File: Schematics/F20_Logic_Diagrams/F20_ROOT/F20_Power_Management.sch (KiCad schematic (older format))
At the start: 9 parts, among them U11 Battery, U12 Cutoff_Switch, U13 Alternator, U14 Rectifier, U15 Starter_Relay, U16 Starter_Motor

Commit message: Added PDM Layout guide, updated Powertrain wiring, added a Master Connector Pinout guide, added TOC to LogicDiagrams pdf and rearranged them a bit.
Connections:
- new net: S1.~, U15.~ (Start)
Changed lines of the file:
@@
 $Descr A 11000 8500
 encoding utf-8
-Sheet 10 18
+Sheet 2 18
 Title "Fuses and Relays"
 Date "2020-01-28"

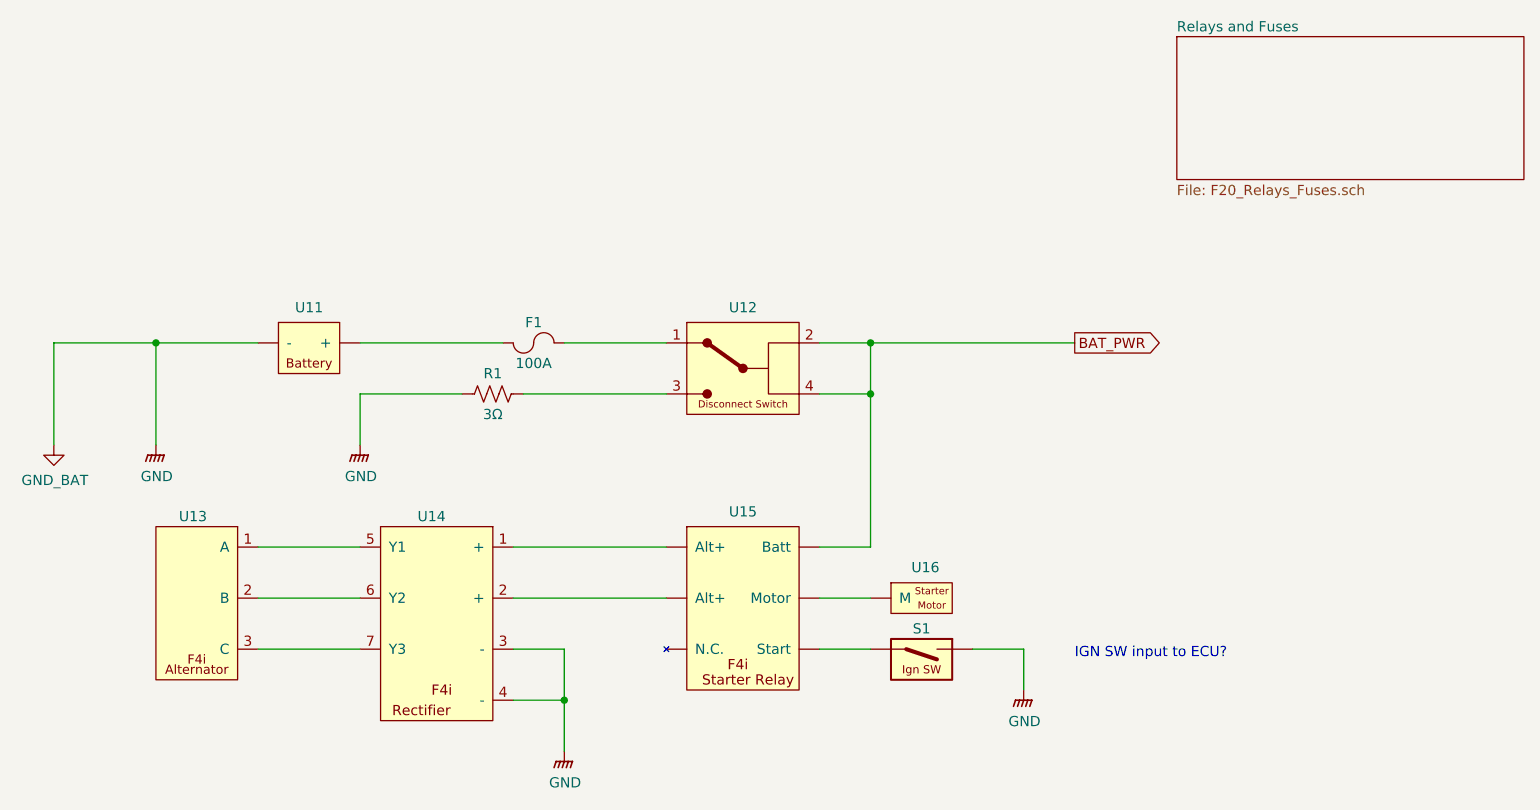
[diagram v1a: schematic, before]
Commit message: Re-annotated Logic Diagrams, pulled a BOM list based on Logic Diagrams
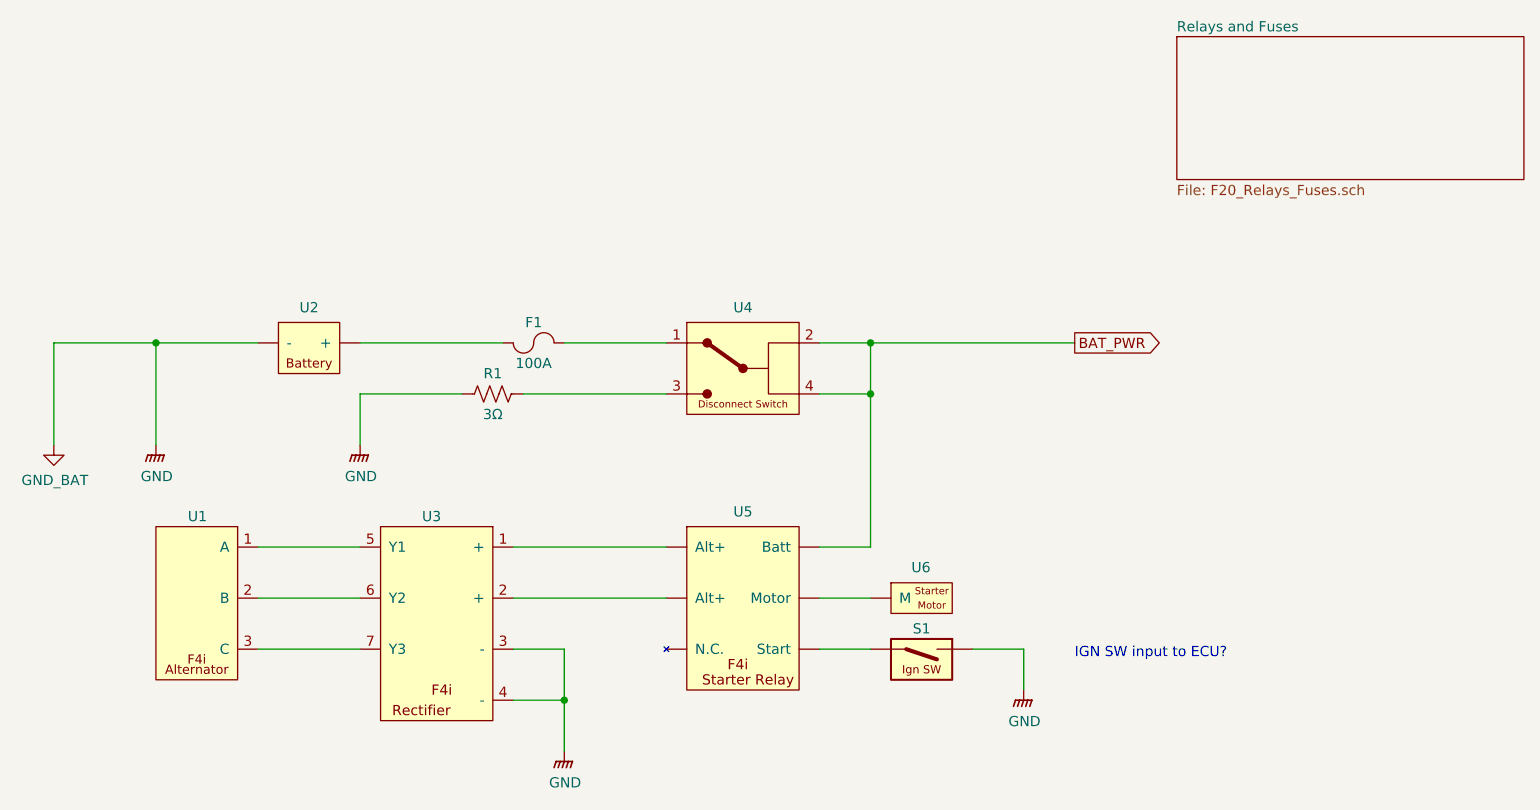
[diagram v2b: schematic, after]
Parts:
- renumbered U13 to U1, U11 to U2, U14 to U3, U12 to U4, U15 to U5, U16 to U6
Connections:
- new net: S1.~, U5.~ (Start)
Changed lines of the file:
@@
 BAT_PWR
 $Comp
-L FSAE_Library:Battery U11
+L FSAE_Library:Battery U2
 U 1 1 5E233AF7
 P 4000 3000
-F 0 "U11" H 3750 3173 50  0000 C CNN
+F 0 "U2" H 3750 3173 50  0000 C CNN
 F 1 "Battery" H 3750 3150 50  0001 C CNN
 F 2 "" H 3750 3150 50  0001 C CNN
@@
 	3000 3000 3500 3000
 $Comp
-L FSAE_Library:Cutoff_Switch U12
+L FSAE_Library:Cutoff_Switch U4
 U 1 1 5E237569
 P 5500 3000
-F 0 "U12" H 5875 3173 50  0000 C CNN
+F 0 "U4" H 5875 3173 50  0000 C CNN
 F 1 "Cutoff_Switch" H 5850 3150 50  0001 C CNN
 F 2 "" H 5850 3150 50  0001 C CNN
@@
 	4000 4000 3500 4000
 $Comp
-L FSAE_Library:Alternator U13
+L FSAE_Library:Alternator U?
 U 1 1 5E21541A
 P 3500 4000
-AR Path="/5E21541A" Ref="U13"  Part="1"
-AR Path="/5E1D1A8A/5E21541A" Ref="U13"  Part="1"
-F 0 "U13" H 3750 4150 50  0000 L CNN
+AR Path="/5E21541A" Ref="U?"  Part="1"
+AR Path="/5E1D1A8A/5E21541A" Ref="U1"  Part="1"
+F 0 "U1" H 3750 4150 50  0000 L CNN
 F 1 "Alternator" H 3800 4150 50  0001 C CNN
 F 2 "" H 3800 4150 50  0001 C CNN
@@
 $EndComp
 $Comp
-L FSAE_Library:Rectifier U14
+L FSAE_Library:Rectifier U3
 U 1 1 5E21334A
 P 4750 4000
-F 0 "U14" H 5150 4150 50  0000 C CNN
+F 0 "U3" H 5150 4150 50  0000 C CNN
 F 1 "Rectifier" H 5000 4150 50  0001 C CNN
 F 2 "" H 5250 4500 50  0001 C CNN
@@
 $EndComp
 $Comp
-L FSAE_Library:Starter_Relay U15
+L FSAE_Library:Starter_Relay U5
 U 1 1 5E3285A1
 P 5500 4000
-F 0 "U15" H 5875 4173 50  0000 C CNN
+F 0 "U5" H 5875 4173 50  0000 C CNN
 F 1 "Starter_Relay" H 5750 4150 50  0001 C CNN
 F 2 "" H 6000 4500 50  0001 C CNN
@@
 Connection ~ 6500 3250
 $Comp
-L FSAE_Library:Starter_Motor U16
+L FSAE_Library:Starter_Motor U6
 U 1 1 5E3347A8
 P 6500 4250
-F 0 "U16" H 6700 4400 50  0000 L CNN
+F 0 "U6" H 6700 4400 50  0000 L CNN
 F 1 "Starter_Motor" H 6750 4400 50  0001 C CNN
 F 2 "" H 6750 4400 50  0001 C CNN
@@
 IGN SW input to ECU?
 $Comp
-L FSAE_Library:GND #PWR011
+L FSAE_Library:GND #PWR03
 U 1 1 5E3B4E50
 P 4000 3500
-F 0 "#PWR011" H 4000 3300 50  0001 C CNN
+F 0 "#PWR03" H 4000 3300 50  0001 C CNN
 F 1 "GND" H 4004 3346 50  0000 C CNN
 F 2 "" H 4000 3450 50  0001 C CNN
@@
 $EndComp
 $Comp
-L FSAE_Library:GND #PWR013
+L FSAE_Library:GND #PWR04
 U 1 1 5E3B6858
 P 5000 5000
-F 0 "#PWR013" H 5000 4800 50  0001 C CNN
+F 0 "#PWR04" H 5000 4800 50  0001 C CNN
 F 1 "GND" H 5004 4846 50  0000 C CNN
 F 2 "" H 5000 4950 50  0001 C CNN
@@
 $EndComp
 $Comp
-L FSAE_Library:GND #PWR012
+L FSAE_Library:GND #PWR05
 U 1 1 5E3B6F4B
 P 7250 4700
-F 0 "#PWR012" H 7250 4500 50  0001 C CNN
+F 0 "#PWR05" H 7250 4500 50  0001 C CNN
 F 1 "GND" H 7254 4546 50  0000 C CNN
 F 2 "" H 7250 4650 50  0001 C CNN
@@
 $EndComp
 $Comp
-L FSAE_Library:GND #PWR010
+L FSAE_Library:GND #PWR02
 U 1 1 5E3B7E28
 P 3000 3500
-F 0 "#PWR010" H 3000 3300 50  0001 C CNN
+F 0 "#PWR02" H 3000 3300 50  0001 C CNN
 F 1 "GND" H 3004 3346 50  0000 C CNN
 F 2 "" H 3000 3450 50  0001 C CNN
@@
 $EndComp
 $Comp
-L FSAE_Library:GND_BAT #PWR09
+L FSAE_Library:GND_BAT #PWR01
 U 1 1 5E3B8350
 P 2500 3500
-F 0 "#PWR09" H 2500 3250 50  0001 C CNN
+F 0 "#PWR01" H 2500 3250 50  0001 C CNN
 F 1 "GND_BAT" H 2505 3327 50  0000 C CNN
 F 2 "" H 2500 3500 50  0001 C CNN
